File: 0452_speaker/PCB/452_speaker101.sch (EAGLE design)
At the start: 27 parts

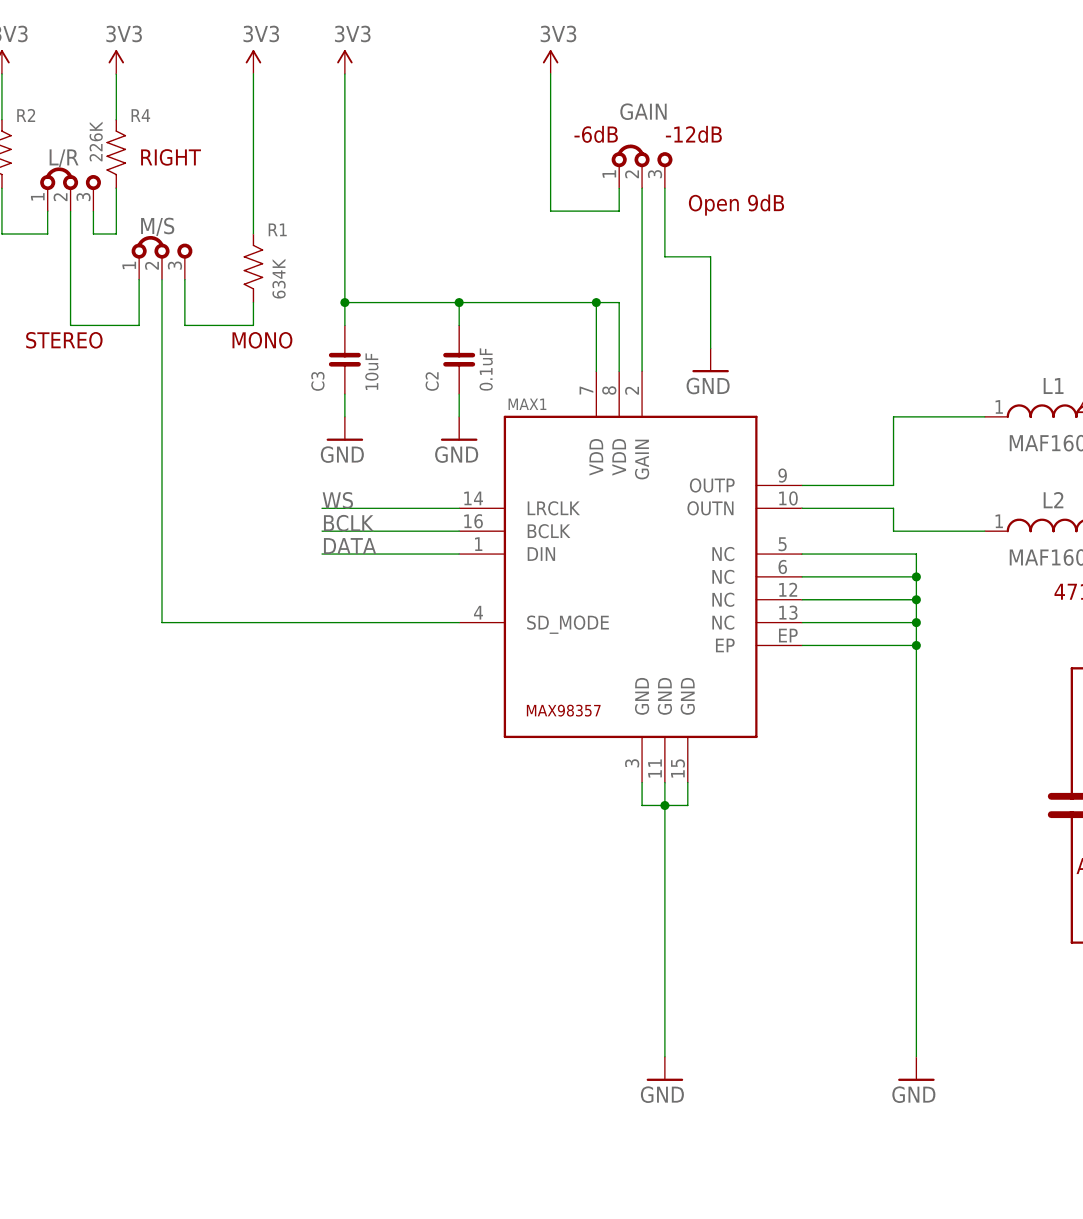
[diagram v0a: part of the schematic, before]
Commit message: #452 IC間隔調整
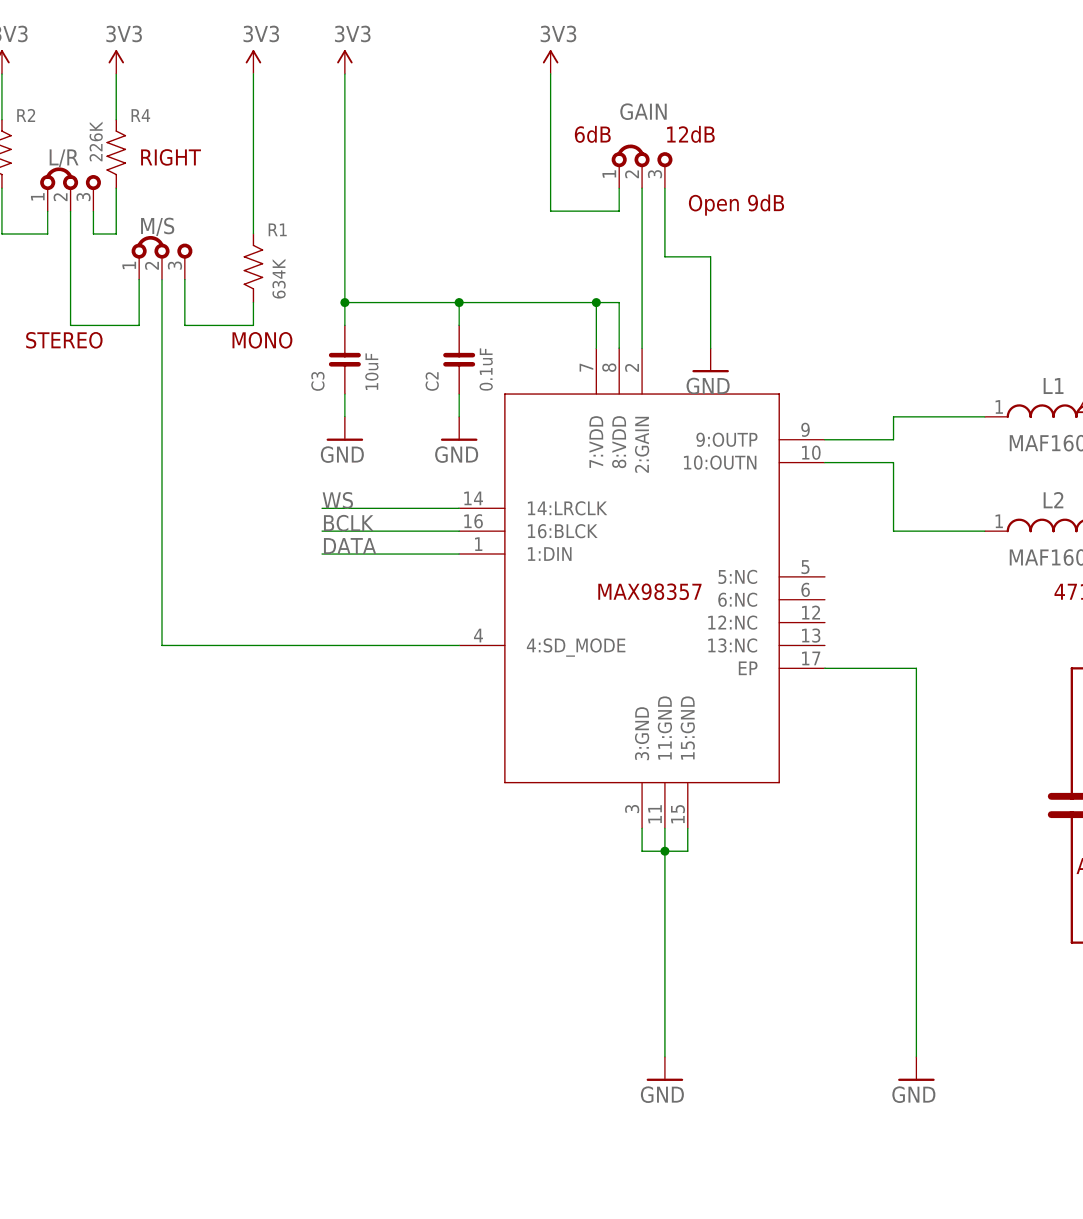
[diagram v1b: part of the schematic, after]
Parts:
- removed MAX1: MA-MAX98357, FaBo-Mems:MA-MAX98357
- added U$2: MAX98357A,B, FaBo-AudioIC:MAX98357A,B
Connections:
- removed net N$5: GAING$1.2, MAX1.GAIN
- new net N$4: GAING$1.2, U$2.2:GAIN
- net 3V3: now also U$2.7:VDD, U$2.8:VDD; no longer MAX1.VDD@7, MAX1.VDD@8
- net BCLK: now also U$2.16:BLCK; no longer MAX1.BCLK
- net DATA: now also U$2.1:DIN; no longer MAX1.DIN
- net GND: now also U$2.11:GND, U$2.15:GND, U$2.3:GND, U$2.EP; no longer MAX1.EP, MAX1.GND@11, MAX1.GND@15, MAX1.GND@3, MAX1.NC@12, MAX1.NC@13, MAX1.NC@5, MAX1.NC@6
- net N$1: now also U$2.10:OUTN; no longer MAX1.OUTN
- net N$2: now also U$2.9:OUTP; no longer MAX1.OUTP
- net N$7: now also U$2.4:SD_MODE; no longer MAX1.SD_MODE
- net WS: now also U$2.14:LRCLK; no longer MAX1.LRCLK
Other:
- note added: "12dB"
- note added: "6dB"
- note removed: "-12dB"
- note removed: "-6dB"
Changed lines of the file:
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@@
 <part name="GND6" library="FaBo-Supply" deviceset="GND" device=""/>
 <part name="I2S" library="FaBo-Template" deviceset="FABO_BRICK_I2S" device=""/>
-<part name="MAX1" library="FaBo-Mems" deviceset="MA-MAX98357" device=""/>
 <part name="GND8" library="FaBo-Supply" deviceset="GND" device=""/>
 <part name="U$4" library="FaBo-Terminal" deviceset="ML-1400-S1" device=""/>
@@
 <part name="GND14" library="FaBo-Supply" deviceset="GND" device=""/>
 <part name="GND15" library="FaBo-Supply" deviceset="GND" device=""/>
+<part name="U$2" library="FaBo-AudioIC" deviceset="MAX98357A,B" device=""/>
 </parts>
 <sheets>
@@
 <text x="248.92" y="119.38" size="1.778" layer="94">+</text>
 <text x="248.92" y="104.14" size="1.778" layer="94">-</text>
-<text x="137.16" y="149.86" size="1.778" layer="94">-6dB</text>
-<text x="147.32" y="149.86" size="1.778" layer="94">-12dB</text>
+<text x="137.16" y="149.86" size="1.778" layer="94">6dB</text>
+<text x="147.32" y="149.86" size="1.778" layer="94">12dB</text>
 <text x="149.86" y="142.24" size="1.778" layer="94">Open 9dB</text>
 <text x="66.04" y="147.32" size="1.778" layer="94">LEFT</text>
@@
 <attribute name="NAME" x="20.32" y="150.368" size="1.778" layer="95"/>
 </instance>
-<instance part="MAX1" gate="G$1" x="139.7" y="96.52" smashed="yes">
-<attribute name="NAME" x="129.794" y="120.142" size="1.27" layer="95"/>
-</instance>
 <instance part="GND8" gate="G$1" x="175.26" y="48.26" smashed="yes">
 <attribute name="VALUE" x="172.466" y="43.18" size="1.778" layer="96"/>
@@
 <attribute name="VALUE" x="213.106" y="132.08" size="1.778" layer="96"/>
 </instance>
+<instance part="U$2" gate="G$1" x="142.24" y="93.98" smashed="yes"/>
 </instances>
 <busses>
@@
 <segment>
 <wire x1="139.7" y1="132.08" x2="142.24" y2="132.08" width="0.1524" layer="91"/>
-<pinref part="MAX1" gate="G$1" pin="VDD@8"/>
-<wire x1="142.24" y1="132.08" x2="142.24" y2="124.46" width="0.1524" layer="91"/>
-<pinref part="MAX1" gate="G$1" pin="VDD@7"/>
-<wire x1="139.7" y1="124.46" x2="139.7" y2="132.08" width="0.1524" layer="91"/>
+<wire x1="142.24" y1="132.08" x2="142.24" y2="127" width="0.1524" layer="91"/>
+<wire x1="139.7" y1="127" x2="139.7" y2="132.08" width="0.1524" layer="91"/>
 <pinref part="3V2" gate="G$1" pin="3V3"/>
 <wire x1="139.7" y1="132.08" x2="124.46" y2="132.08" width="0.1524" layer="91"/>
@@
 <junction x="124.46" y="132.08"/>
 <junction x="139.7" y="132.08"/>
+<pinref part="U$2" gate="G$1" pin="7:VDD"/>
+<pinref part="U$2" gate="G$1" pin="8:VDD"/>
 </segment>
 <segment>
@@
 </segment>
 <segment>
-<pinref part="MAX1" gate="G$1" pin="GND@3"/>
-<wire x1="144.78" y1="78.74" x2="144.78" y2="76.2" width="0.762" layer="91"/>
-<pinref part="MAX1" gate="G$1" pin="GND@15"/>
-<wire x1="144.78" y1="76.2" x2="147.32" y2="76.2" width="0.762" layer="91"/>
-<wire x1="147.32" y1="76.2" x2="149.86" y2="76.2" width="0.762" layer="91"/>
-<wire x1="149.86" y1="76.2" x2="149.86" y2="78.74" width="0.762" layer="91"/>
-<pinref part="MAX1" gate="G$1" pin="GND@11"/>
-<wire x1="147.32" y1="78.74" x2="147.32" y2="76.2" width="0.762" layer="91"/>
 <pinref part="GND2" gate="G$1" pin="GND"/>
-<wire x1="147.32" y1="48.26" x2="147.32" y2="76.2" width="0.762" layer="91"/>
-<junction x="147.32" y="76.2"/>
-</segment>
-<segment>
-<pinref part="MAX1" gate="G$1" pin="NC@5"/>
-<wire x1="162.56" y1="104.14" x2="175.26" y2="104.14" width="0.762" layer="91"/>
-<wire x1="175.26" y1="104.14" x2="175.26" y2="101.6" width="0.762" layer="91"/>
-<pinref part="MAX1" gate="G$1" pin="NC@6"/>
-<wire x1="175.26" y1="101.6" x2="175.26" y2="99.06" width="0.762" layer="91"/>
-<wire x1="175.26" y1="99.06" x2="175.26" y2="96.52" width="0.762" layer="91"/>
-<wire x1="175.26" y1="96.52" x2="175.26" y2="93.98" width="0.762" layer="91"/>
-<wire x1="175.26" y1="93.98" x2="175.26" y2="48.26" width="0.762" layer="91"/>
-<wire x1="162.56" y1="101.6" x2="175.26" y2="101.6" width="0.762" layer="91"/>
-<pinref part="MAX1" gate="G$1" pin="NC@12"/>
-<wire x1="162.56" y1="99.06" x2="175.26" y2="99.06" width="0.762" layer="91"/>
-<pinref part="MAX1" gate="G$1" pin="NC@13"/>
-<wire x1="162.56" y1="96.52" x2="175.26" y2="96.52" width="0.762" layer="91"/>
-<pinref part="MAX1" gate="G$1" pin="EP"/>
-<wire x1="162.56" y1="93.98" x2="175.26" y2="93.98" width="0.762" layer="91"/>
+<wire x1="147.32" y1="48.26" x2="147.32" y2="71.12" width="0.762" layer="91"/>
+<pinref part="U$2" gate="G$1" pin="11:GND"/>
+<pinref part="U$2" gate="G$1" pin="3:GND"/>
+<wire x1="147.32" y1="71.12" x2="147.32" y2="73.66" width="0.762" layer="91"/>
+<wire x1="144.78" y1="73.66" x2="144.78" y2="71.12" width="0.762" layer="91"/>
+<wire x1="144.78" y1="71.12" x2="147.32" y2="71.12" width="0.762" layer="91"/>
+<junction x="147.32" y="71.12"/>
+<pinref part="U$2" gate="G$1" pin="15:GND"/>
+<wire x1="149.86" y1="73.66" x2="149.86" y2="71.12" width="0.762" layer="91"/>
+<wire x1="149.86" y1="71.12" x2="147.32" y2="71.12" width="0.762" layer="91"/>
+</segment>
+<segment>
+<wire x1="175.26" y1="91.44" x2="175.26" y2="48.26" width="0.762" layer="91"/>
 <pinref part="GND8" gate="G$1" pin="GND"/>
-<junction x="175.26" y="101.6"/>
-<junction x="175.26" y="99.06"/>
-<junction x="175.26" y="96.52"/>
-<junction x="175.26" y="93.98"/>
+<pinref part="U$2" gate="G$1" pin="EP"/>
+<wire x1="165.1" y1="91.44" x2="175.26" y2="91.44" width="0.762" layer="91"/>
 </segment>
 <segment>
@@
 </segment>
 <segment>
-<pinref part="MAX1" gate="G$1" pin="LRCLK"/>
 <wire x1="124.46" y1="109.22" x2="109.22" y2="109.22" width="0.1524" layer="91"/>
 <label x="109.22" y="109.22" size="1.778" layer="95"/>
+<pinref part="U$2" gate="G$1" pin="14:LRCLK"/>
 </segment>
 </net>
@@
 </segment>
 <segment>
-<pinref part="MAX1" gate="G$1" pin="BCLK"/>
 <wire x1="124.46" y1="106.68" x2="109.22" y2="106.68" width="0.1524" layer="91"/>
 <label x="109.22" y="106.68" size="1.778" layer="95"/>
+<pinref part="U$2" gate="G$1" pin="16:BLCK"/>
 </segment>
 </net>
@@
 </segment>
 <segment>
-<pinref part="MAX1" gate="G$1" pin="DIN"/>
 <wire x1="124.46" y1="104.14" x2="109.22" y2="104.14" width="0.1524" layer="91"/>
 <label x="109.22" y="104.14" size="1.778" layer="95"/>
+<pinref part="U$2" gate="G$1" pin="1:DIN"/>
 </segment>
 </net>
@@
 <pinref part="L2" gate="G$1" pin="3"/>
 <wire x1="182.88" y1="106.68" x2="172.72" y2="106.68" width="0.1524" layer="91"/>
-<wire x1="172.72" y1="106.68" x2="172.72" y2="109.22" width="0.1524" layer="91"/>
-<pinref part="MAX1" gate="G$1" pin="OUTN"/>
-<wire x1="172.72" y1="109.22" x2="162.56" y2="109.22" width="0.1524" layer="91"/>
+<wire x1="172.72" y1="106.68" x2="172.72" y2="114.3" width="0.1524" layer="91"/>
+<wire x1="172.72" y1="114.3" x2="165.1" y2="114.3" width="0.1524" layer="91"/>
+<pinref part="U$2" gate="G$1" pin="10:OUTN"/>
 </segment>
 </net>
 <net name="N$2" class="0">
 <segment>
-<pinref part="MAX1" gate="G$1" pin="OUTP"/>
-<wire x1="162.56" y1="111.76" x2="172.72" y2="111.76" width="0.1524" layer="91"/>
-<wire x1="172.72" y1="111.76" x2="172.72" y2="119.38" width="0.1524" layer="91"/>
+<wire x1="165.1" y1="116.84" x2="172.72" y2="116.84" width="0.1524" layer="91"/>
+<wire x1="172.72" y1="116.84" x2="172.72" y2="119.38" width="0.1524" layer="91"/>
 <pinref part="L1" gate="G$1" pin="3"/>
 <wire x1="172.72" y1="119.38" x2="182.88" y2="119.38" width="0.1524" layer="91"/>
-</segment>
-</net>
-<net name="N$5" class="0">
-<segment>
-<pinref part="MAX1" gate="G$1" pin="GAIN"/>
-<wire x1="144.78" y1="124.46" x2="144.78" y2="144.78" width="0.1524" layer="91"/>
-<pinref part="GAIN" gate="G$1" pin="2"/>
+<pinref part="U$2" gate="G$1" pin="9:OUTP"/>
 </segment>
 </net>
 <net name="N$7" class="0">
 <segment>
-<pinref part="MAX1" gate="G$1" pin="SD_MODE"/>
 <pinref part="M/S" gate="G$1" pin="2"/>
-<wire x1="124.46" y1="96.52" x2="91.44" y2="96.52" width="0.1524" layer="91"/>
-<wire x1="91.44" y1="96.52" x2="91.44" y2="134.62" width="0.1524" layer="91"/>
+<wire x1="124.46" y1="93.98" x2="91.44" y2="93.98" width="0.1524" layer="91"/>
+<wire x1="91.44" y1="93.98" x2="91.44" y2="134.62" width="0.1524" layer="91"/>
+<pinref part="U$2" gate="G$1" pin="4:SD_MODE"/>
 </segment>
 </net>
@@
 </segment>
 </net>
+<net name="N$4" class="0">
+<segment>
+<pinref part="U$2" gate="G$1" pin="2:GAIN"/>
+<pinref part="GAIN" gate="G$1" pin="2"/>
+<wire x1="144.78" y1="127" x2="144.78" y2="144.78" width="0.1524" layer="91"/>
+</segment>
+</net>
